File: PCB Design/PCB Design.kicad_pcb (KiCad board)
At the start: 2 copper layers, 76.5 x 46.5 mm, 23 parts, among them J1 Conn_01x01_Pin, J10 Conn_01x01_Pin, J11 Conn_01x01_Pin, J12 Conn_01x01_Pin, J13 Conn_01x01_Pin, J2 Conn_01x01_Pin, J3 Conn_01x01_Pin, J4 Conn_01x01_Pin, J5 Conn_01x01_Pin, J6 Conn_01x01_Pin, J7 Conn_01x01_Pin, J8 Conn_01x01_Pin, J9 Conn_01x01_Pin, SW1 SW_SP3T, SW2 SW_DPDT_x2

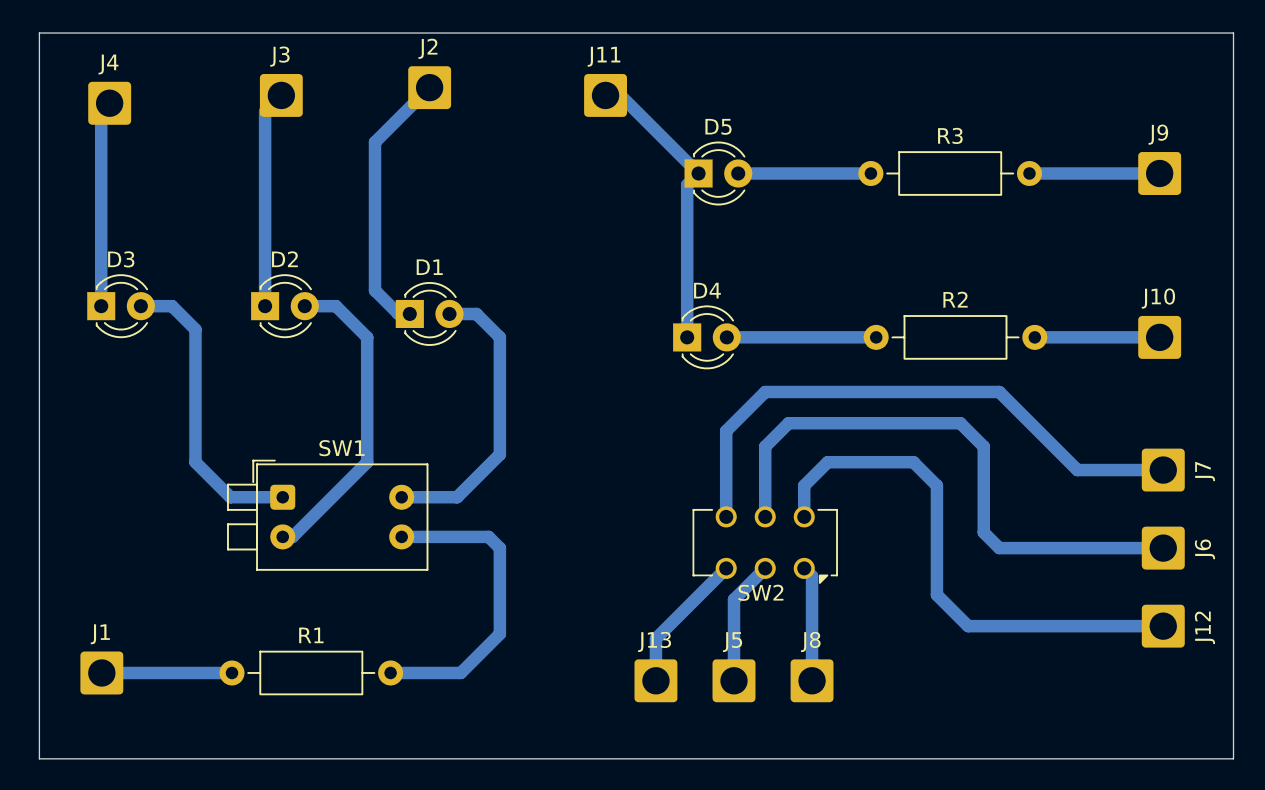
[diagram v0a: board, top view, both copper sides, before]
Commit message: altered schematic and PCB layout for new SPDT switches
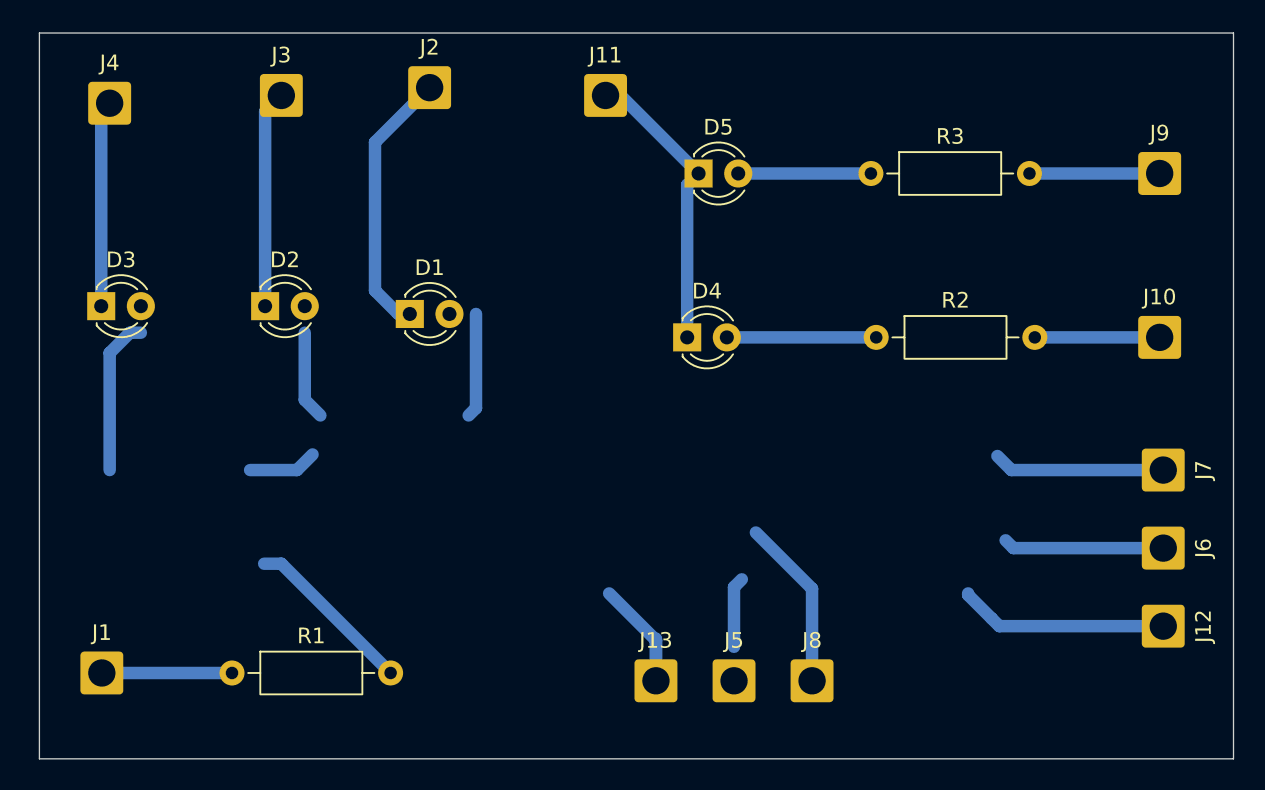
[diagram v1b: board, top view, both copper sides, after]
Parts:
- removed SW1: SW_SP3T, Button_Switch_THT:SW_DIP_SPSTx02_Piano_10.8x6.64mm_W7.62mm_P2.54mm
- removed SW2: SW_DPDT_x2, Button_Switch_THT:SW_CK_JS202011CQN_DPDT_Straight
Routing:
- net (no net): track 0.00 -> 31.4 mm
- net Net-(J6-Pin_1): track 37.2 -> 10.3 mm
- net Net-(J7-Pin_1): track 36.6 -> 11.0 mm
- net Net-(J12-Pin_1): track 34.1 -> 13.4 mm
- net Net-(D2-A): track 20.2 -> 0.00 mm
- net Net-(D3-A): track 19.1 -> 0.00 mm
- net Net-(D1-A): track 18.8 -> 0.00 mm
- net Net-(SW1-B): track 20.1 -> 11.0 mm
- net Net-(J5-Pin_1): track 8.03 -> 0.00 mm
- net Net-(J8-Pin_1): track 7.41 -> 11.0 mm

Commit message: adding footprint for the swithces
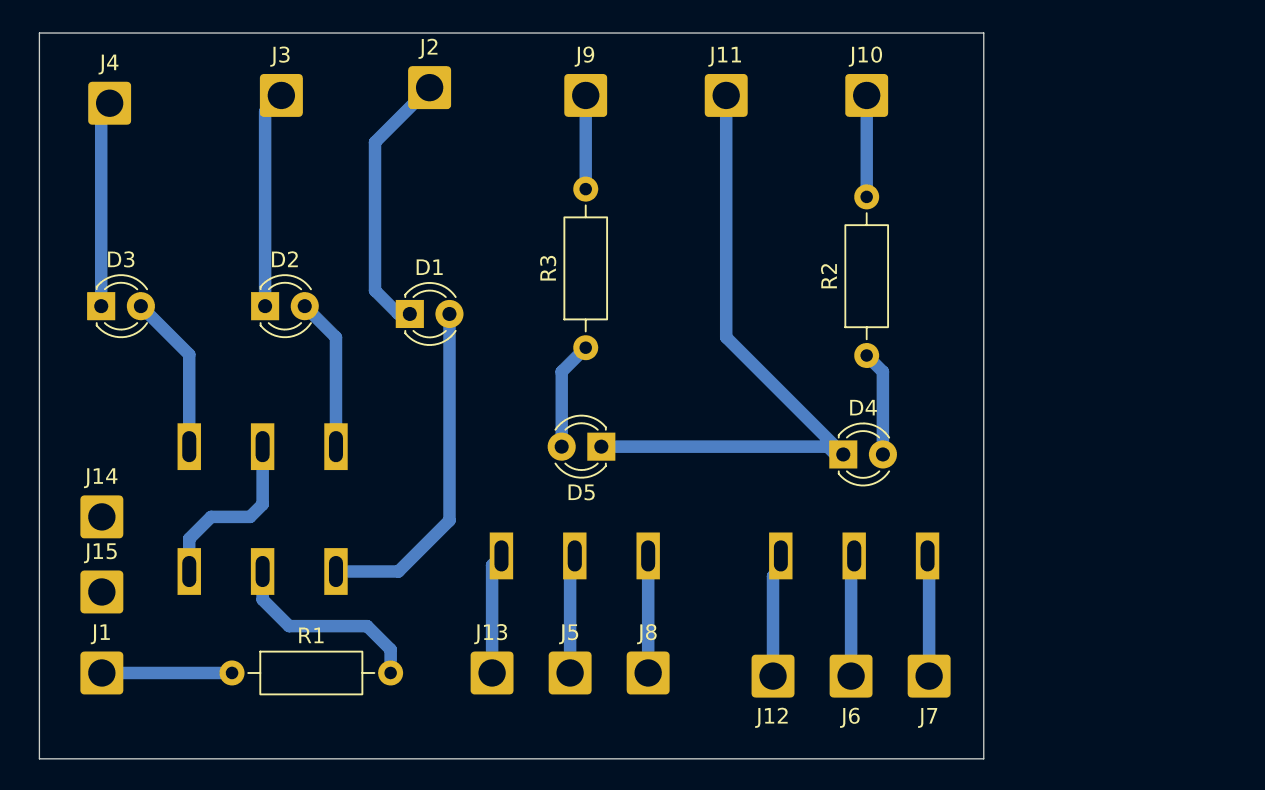
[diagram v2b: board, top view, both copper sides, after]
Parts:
- added J14: Conn_01x01_Pin, Connector_Wire:SolderWire-1sqmm_1x01_D1.4mm_OD2.7mm, F.Cu at (86.5, 82.0)
- added J15: Conn_01x01_Pin, Connector_Wire:SolderWire-1sqmm_1x01_D1.4mm_OD2.7mm, F.Cu at (86.5, 86.8)
- added SW1: SW_SPDT, footprints :SW_SPDT, F.Cu at (96.8, 85.5)
- added SW2: SW_SPDT, footprints :SW_SPDT, F.Cu at (96.8, 77.5)
- added SW3: SW_SPDT, footprints :SW_SPDT, F.Cu at (116.8, 84.5)
- added SW4: SW_SPDT, footprints :SW_SPDT, F.Cu at (134.7, 84.5)
- moved J9 37.1 mm to (117.5, 55.0)
- moved J12 25.2 mm to (129.5, 92.2), turned to 180 degrees
- moved J10 24.3 mm to (135.5, 55.0)
- moved J6 21.6 mm to (134.5, 92.2), turned to 180 degrees
- moved R3 21.4 mm to (117.5, 71.2), turned to 90 degrees
- moved J7 20.0 mm to (139.5, 92.2), turned to 180 degrees
- moved D5 18.6 mm to (118.5, 77.5), turned to 180 degrees
- moved D4 12.5 mm to (134.0, 78.0)
- moved J13 10.5 mm to (111.5, 92.0)
- moved J5 10.5 mm to (116.5, 92.0)
- moved J8 10.5 mm to (121.5, 92.0)
- moved J11 7.73 mm to (126.5, 55.0)
- moved R2 1.31 mm to (135.5, 71.7), turned to 90 degrees
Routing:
- net (no net): track 31.4 -> 0.00 mm
- net Net-(D4-K): track 18.8 -> 41.8 mm
- net Net-(D1-A): track 0.00 -> 21.9 mm
- net Net-(SW1-A): track 0.00 -> 11.4 mm
- net Net-(D3-A): track 0.00 -> 10.3 mm
- net Net-(D2-A): track 0.00 -> 9.83 mm
- net Net-(J5-Pin_1): track 0.00 -> 7.62 mm
- net Net-(J12-Pin_1): track 13.4 -> 7.25 mm
- net Net-(J7-Pin_1): track 11.0 -> 7.00 mm
- net Net-(J8-Pin_1): track 11.0 -> 7.50 mm
- net Net-(J6-Pin_1): track 10.3 -> 7.12 mm
- net Net-(D4-A): track 9.57 -> 6.77 mm
- net Net-(J9-Pin_1): track 8.34 -> 6.00 mm
- net Net-(SW1-B): track 11.0 -> 12.8 mm
- net Net-(J13-Pin_1): track 9.54 -> 7.75 mm
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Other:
- board size 76.5 x 46.5 mm -> 60.5 x 46.5 mm

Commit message: completed main pcb design
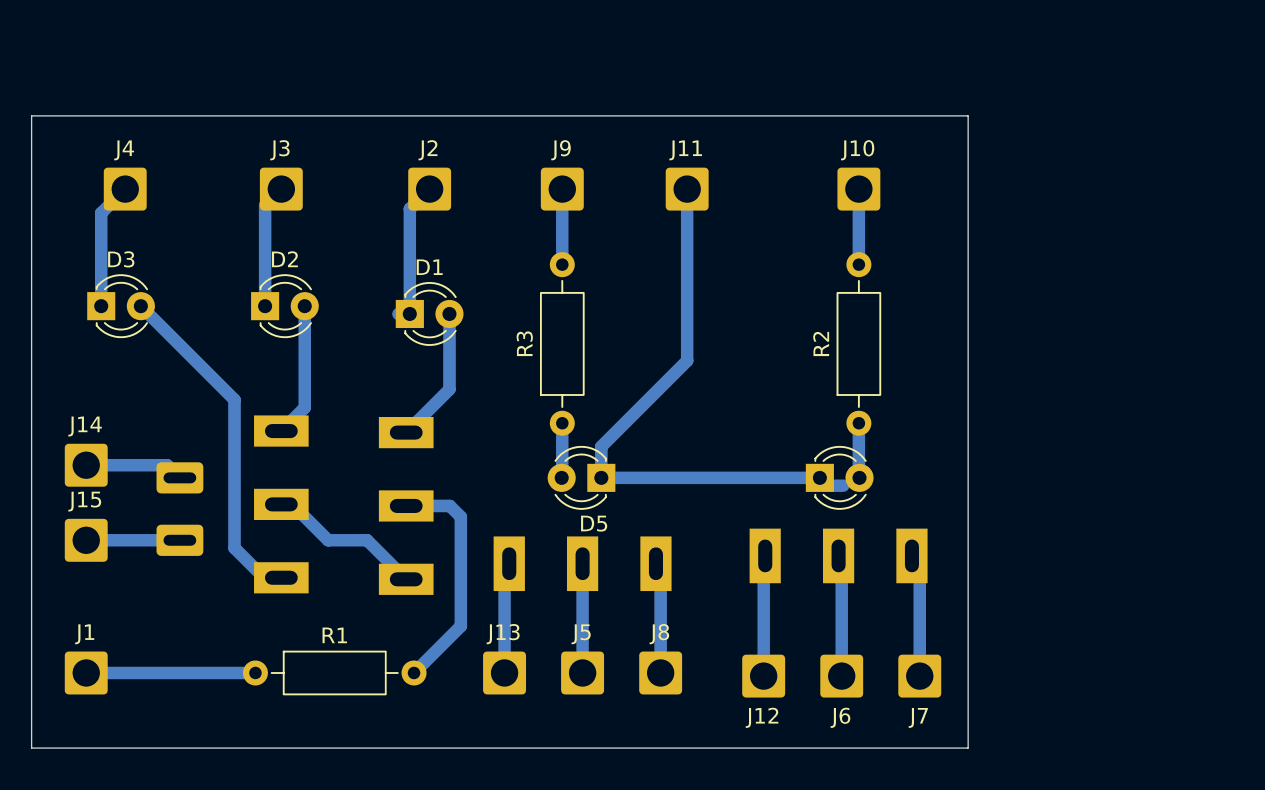
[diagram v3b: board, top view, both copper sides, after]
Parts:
- added SW5: pushbuttonfoot, buttonfootprint:Untitled, F.Cu at (91.5, 79.5)
- moved SW1 10.1 mm to (106.0, 81.3), turned to 180 degrees
- moved J11 6.50 mm to (124.0, 61.0)
- moved J2 6.50 mm to (107.5, 61.0)
- moved J9 6.18 mm to (116.0, 61.0)
- moved J10 6.02 mm to (135.0, 61.0)
- moved J3 6.00 mm to (98.0, 61.0)
- moved J4 5.59 mm to (88.0, 61.0)
- moved R3 5.07 mm to (116.0, 76.0)
- moved R2 4.37 mm to (135.0, 76.0)
- moved SW2 3.89 mm to (98.0, 81.2), turned to 180 degrees
- moved J14 3.46 mm to (85.5, 78.7)
- moved J15 3.46 mm to (85.5, 83.5)
- moved D4 2.12 mm to (132.5, 79.5)
- moved D5 2.00 mm to (118.5, 79.5)
- moved R1 1.50 mm to (96.3, 92.0)
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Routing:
- net Net-(D1-A): track 21.9 -> 8.75 mm
- net Net-(D3-A): track 10.3 -> 21.8 mm
- net Net-(D1-K): track 17.3 -> 9.26 mm
- net Net-(D4-K): track 41.8 -> 35.3 mm
- net Net-(J14-Pin_1): track 0.00 -> 6.34 mm
- net Net-(D2-K): track 13.9 -> 7.93 mm
- net Net-(J15-Pin_1): track 0.00 -> 6.00 mm
- net Net-(D3-K): track 13.2 -> 8.14 mm
- net Net-(D5-A): track 6.98 -> 3.52 mm
- net Net-(D4-A): track 6.77 -> 3.47 mm
- net Net-(J1-Pin_1): track 8.34 -> 10.8 mm
- net Net-(SW1-B): track 12.8 -> 15.0 mm
- net Net-(J10-Pin_1): track 6.50 -> 4.84 mm
- net Net-(SW1-A): track 11.4 -> 9.99 mm
- net Net-(D2-A): track 9.83 -> 8.62 mm
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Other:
- board size 60.5 x 46.5 mm -> 60 x 40.5 mm

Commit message: added Gerber files
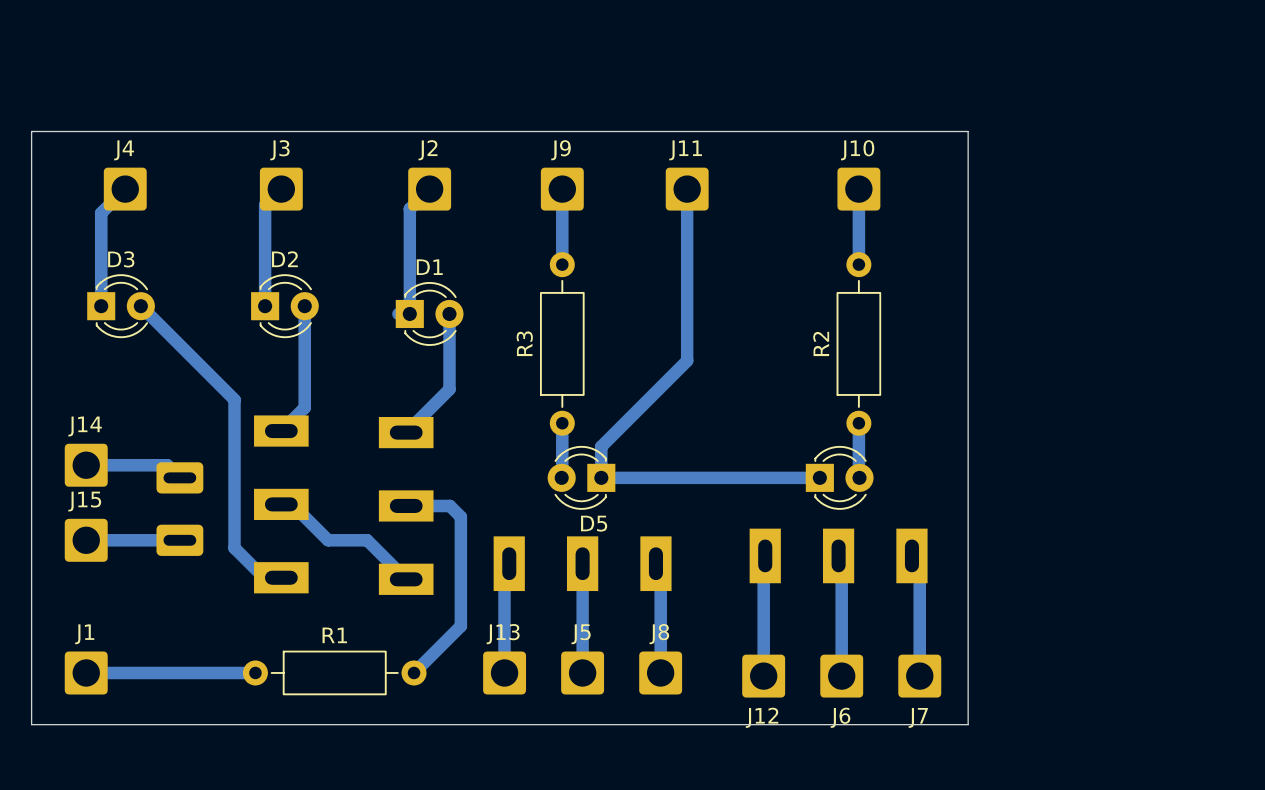
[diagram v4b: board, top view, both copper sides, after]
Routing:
- net Net-(D4-K): track 35.3 -> 34.8 mm
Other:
- board size 60 x 40.5 mm -> 60 x 38 mm
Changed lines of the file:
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@@
 		(tenting front back)
 		(pcbplotparams
-			(layerselection 0x00000000_00000000_55555555_5755f5ff)
-			(plot_on_all_layers_selection 0x00000000_00000000_00000000_00000000)
+			(layerselection 0x00000000_00000000_55555555_55555555)
+			(plot_on_all_layers_selection 0x00000000_00000000_00000000_02000000)
 			(disableapertmacros no)
 			(usegerberextensions no)
@@
 			(outputformat 1)
 			(mirror no)
-			(drillshape 1)
+			(drillshape 0)
 			(scaleselection 1)
-			(outputdirectory "")
+			(outputdirectory "PCB Submission/")
 		)
 	)
@@
 	)
 	(gr_rect
-		(start 82 56.31)
-		(end 142 96.81)
+		(start 82 57.31)
+		(end 142 95.31)
 		(stroke
 			(width 0.05)
@@
 		(width 0.8)
 		(layer "B.Cu")
-		(net 8)
-	)
-	(segment
-		(start 134 80)
-		(end 133.5 80)
-		(width 0.8)
-		(layer "B.Cu")
